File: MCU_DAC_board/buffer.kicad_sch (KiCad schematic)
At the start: 2 parts, among them U4 LM2902PWR

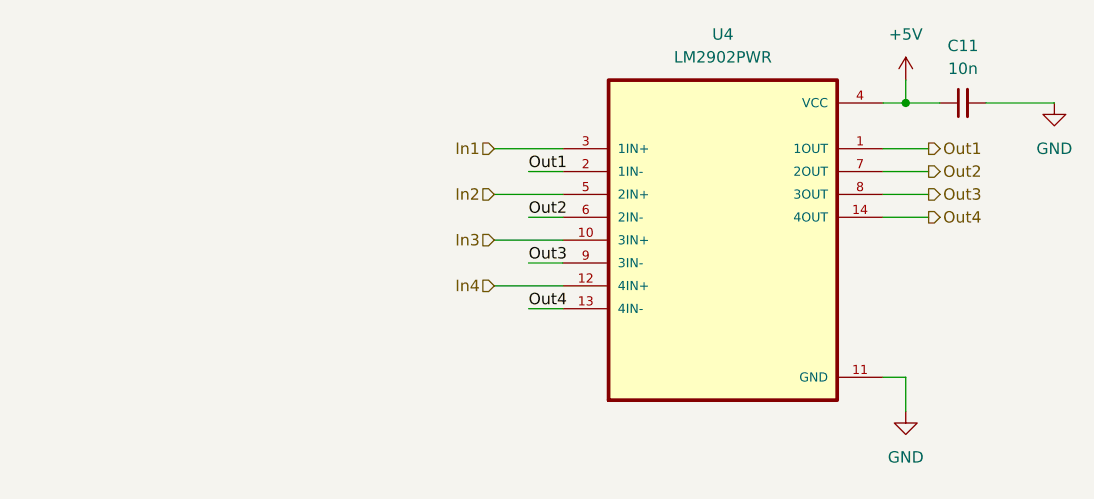
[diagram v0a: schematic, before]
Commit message: Added 2.5V regulator circuit, jumpers on buffers
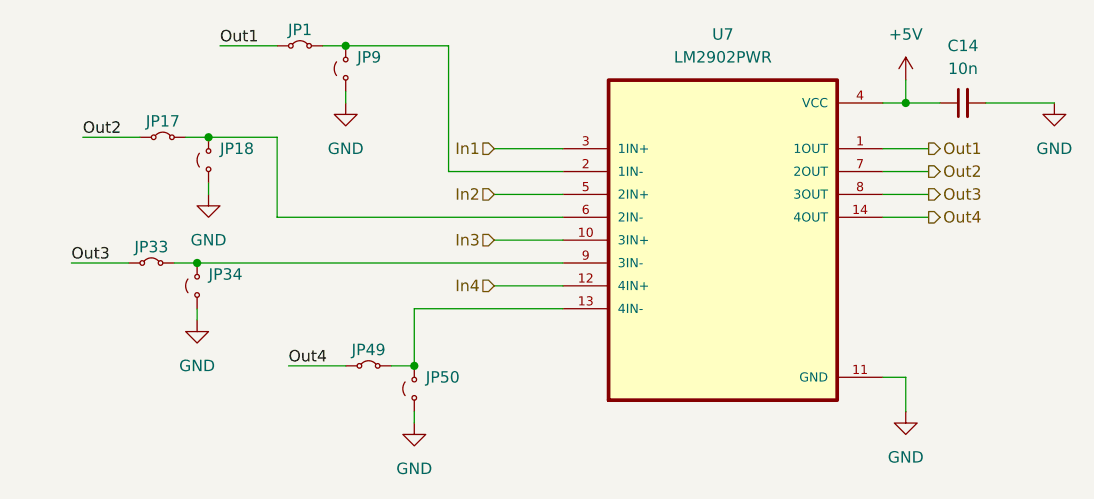
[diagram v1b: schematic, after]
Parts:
- added JP1, JP17, JP33, JP49: ~, symbol Jumper:Jumper_2_Small_Bridged
- added JP18, JP34, JP50, JP9: Jumper_2_Small_Open, symbol Jumper:Jumper_2_Small_Open
- renumbered C11 to C14, U4 to U7
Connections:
- net GND: now also JP18.1 (A), JP34.1 (A), JP50.1 (A), JP9.1 (A)
- net Out1: now also JP1.1 (A); no longer U7.2 (1IN-)
- net Out2: now also JP17.1 (A); no longer U7.6 (2IN-)
- net Out3: now also JP33.1 (A); no longer U7.9 (3IN-)
- net Out4: now also JP49.1 (A); no longer U7.13 (4IN-)
- new net: JP49.2 (B), JP50.2 (B), U7.13 (4IN-)
- new net: JP17.2 (B), JP18.2 (B), U7.6 (2IN-)
- new net: JP1.2 (B), JP9.2 (B), U7.2 (1IN-)
- new net: JP33.2 (B), JP34.2 (B), U7.9 (3IN-)

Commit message: Added filtering between DAC and amp, power receptacles
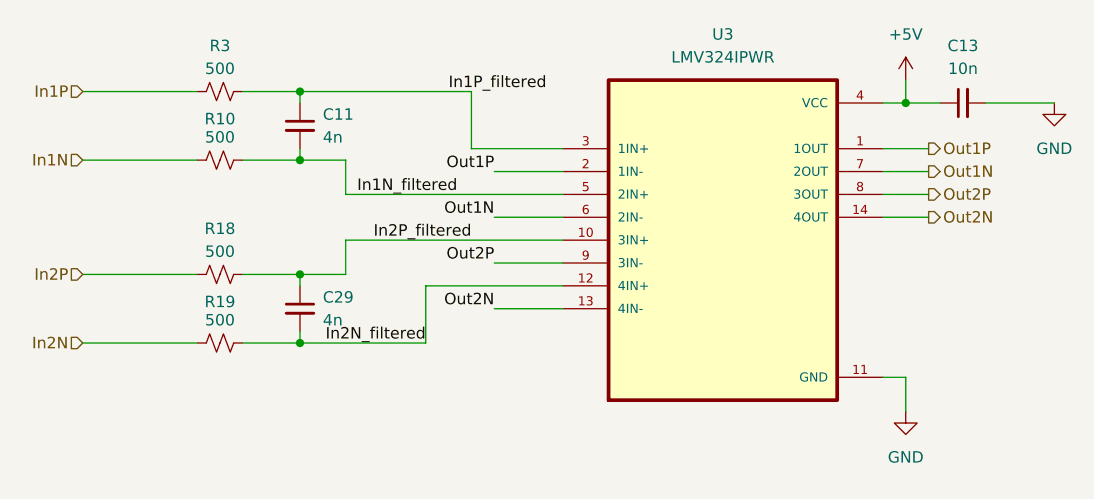
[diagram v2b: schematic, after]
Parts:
- removed JP1, JP17, JP33, JP49: ~, symbol Jumper:Jumper_2_Small_Bridged
- removed JP18, JP34, JP50, JP9: Jumper_2_Small_Open, symbol Jumper:Jumper_2_Small_Open
- added C11, C29: 4n, symbol Device:C_Small
- added R10, R18, R19, R3: 500, symbol Device:R_Small_US
- U3: renamed from U7; value LM2902PWR -> LMV324IPWR
- renumbered C14 to C13
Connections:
- net Out1 is gone; now on net Out1P: U3.1 (1OUT)
- net Out2 is gone; now on net Out1N: U3.7 (2OUT)
- net Out3 is gone; now on net Out2P: U3.8 (3OUT)
- net Out4 is gone; now on net Out2N: U3.14 (4OUT)
- net Out2N: now reaches U3.13 (4IN-)
- net Out1N: now reaches U3.6 (2IN-)
- net Out1P: now reaches U3.2 (1IN-)
- net Out2P: now reaches U3.9 (3IN-)
- net In1 renamed In1P_filtered
- net In1P_filtered: now also C11.1, R3.2
- net In2 renamed In1N_filtered
- net In1N_filtered: now also C11.2, R10.2
- net In3 renamed In2P_filtered
- net In2P_filtered: now also C29.1, R18.2
- net In4 renamed In2N_filtered
- net In2N_filtered: now also C29.2, R19.2
- new net In1N: R10.1
- new net In1P: R3.1
- new net In2N: R19.1
- new net In2P: R18.1

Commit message: Removed buffers on DAC board
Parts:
- renumbered C29 to C12, R3 to R2, R10 to R3, R18 to R4, R19 to R5
